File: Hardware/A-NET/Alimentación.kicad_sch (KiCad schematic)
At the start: 19 parts, among them J1 BAT, U1 TPS563252DRLR

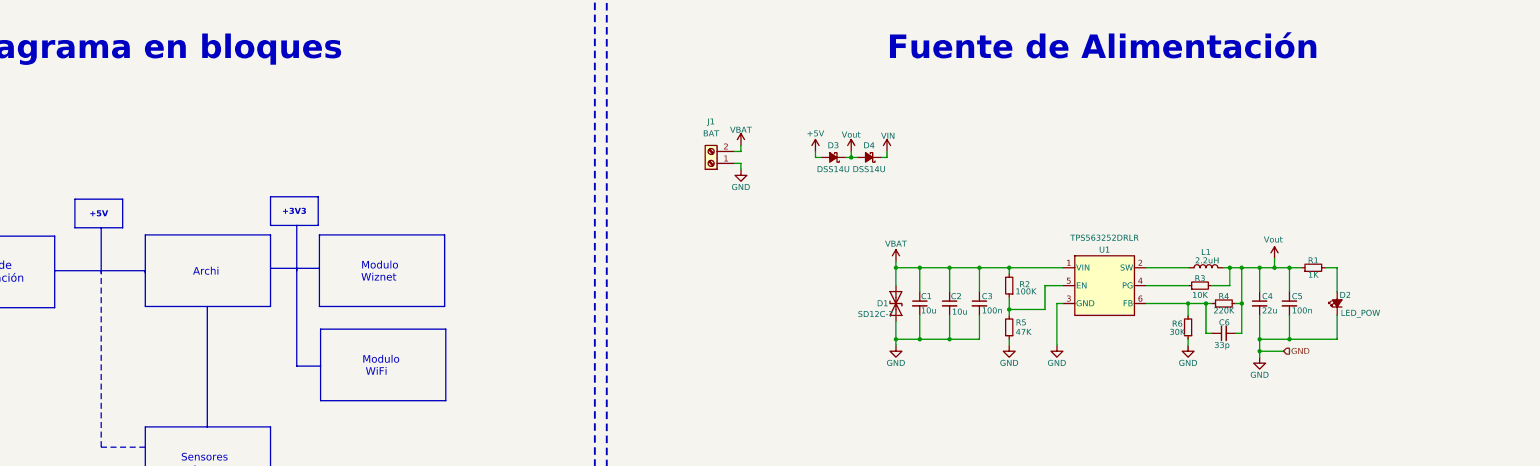
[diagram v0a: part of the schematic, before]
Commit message: add digikey | add POE
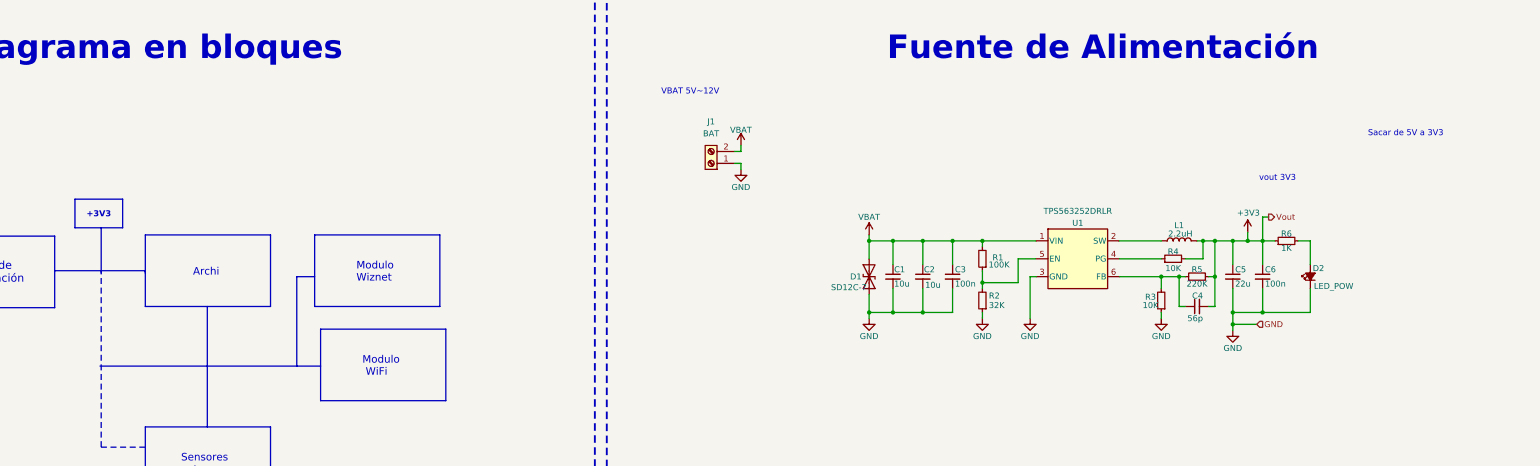
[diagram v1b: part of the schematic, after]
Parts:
- removed D3, D4: DSS14U, Diode_SMD:D_SOD-123F, symbol Device:D_Schottky_Small_Filled
- C4: renamed from C6; value 33p -> 56p
- J1: PartNumber (none) -> VI0221520000G; PurchaseLink (none) -> https://www.digikey.de/en/products/detail/amphenol-anytek/V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
- R2: renamed from R5; value 47K -> 32K
- R3: renamed from R6; value 30K -> 10K; PartNumber RC0603FR-0730KL -> RCS060310K0JNEA; PurchaseLink https://www.digikey.com/en/products/detail/yageo/RC0603FR-0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 -> https://www.digikey.de/en/products/detail/vishay-dale/RCS06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
- R4: renamed from R3; PartNumber RC0603FR-0710KL -> RCS060310K0JNEA; PurchaseLink https://www.digikey.com/en/products/detail/yageo/RC0603FR-0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 -> https://www.digikey.de/en/products/detail/vishay-dale/RCS06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
- R6: renamed from R1; PartNumber RC0603FR-071KL -> RCS06031K00FKEA; PurchaseLink https://www.digikey.com/en/products/detail/yageo/RC0603FR-0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 -> https://www.digikey.de/en/products/detail/vishay-dale/RCS06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
- renumbered C4 to C5, C5 to C6, R2 to R1, R4 to R5
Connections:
- net Vout renamed +3V3
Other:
- note added: "Sacar de 5V a 3V3"
- note added: "VBAT 5V~12V"
- note added: "vout 3V3"
- note removed: "+5V"
- moved on the sheet: C1, C2, C3, C4, C5, C6, D1, D2, L1, R1, R2, R3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

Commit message: Add files via upload
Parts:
- U1: footprint NSARCHI:SOT6_DRL_TEX-L -> anetLib:SOT6_DRL_TEX-L
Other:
- note removed: "Sacar de 5V a 3V3"
- note removed: "VBAT 5V~12V"
- note removed: "vout 3V3"
- moved on the sheet: C1, C2, C3, C4, C5, C6, D1, D2, J1, L1, R1, R2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

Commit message: #V.1
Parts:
- R6: PurchaseLink https://www.digikey.de/en/products/detail/vishay-dale/RCS06031K00FKEA/5866934 -> https://www.digikey.de/en/products/detail/vishay-dale/RCS06035K10FKEA/5868559
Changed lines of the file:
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@@
 			)
 		)
-		(property "PurchaseLink" "https://www.digikey.de/en/products/detail/vishay-dale/RCS06031K00FKEA/5866934"
+		(property "PurchaseLink" "https://www.digikey.de/en/products/detail/vishay-dale/RCS06035K10FKEA/5868559"
 			(at 346.71 67.945 0)
 			(effects
